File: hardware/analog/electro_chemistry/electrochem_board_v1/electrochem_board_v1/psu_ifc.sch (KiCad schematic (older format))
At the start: 1 part

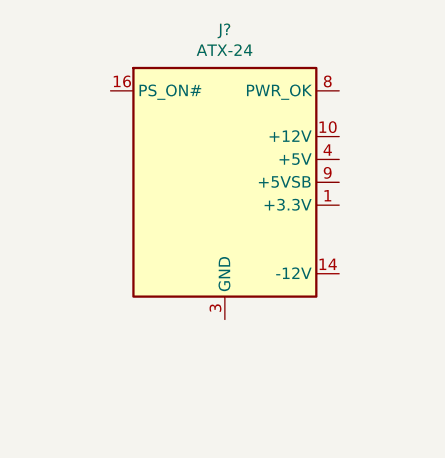
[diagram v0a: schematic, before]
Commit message: Electrochemistry board: preparing the layout
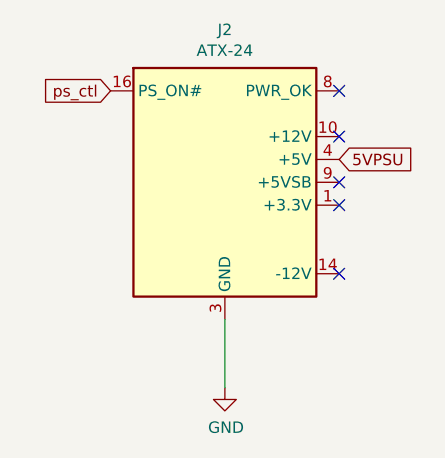
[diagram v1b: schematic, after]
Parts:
- J2: renamed from J?; footprint (none) -> Connector_Molex:Molex_Mini-Fit_Jr_5566-24A_2x12_P4.20mm_Vertical
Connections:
- net GND: now reaches J2.15 (GND), J2.17 (GND), J2.18 (GND), J2.19 (GND), J2.24 (GND), J2.3 (GND), J2.5 (GND), J2.7 (GND)
- net ps_ctl: now reaches J2.16 (PS_ON#)
- net 5VPSU: now reaches J2.21 (+5V), J2.22 (+5V), J2.23 (+5V), J2.4 (+5V), J2.6 (+5V)
- no-connect marks 0 -> 5
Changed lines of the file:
@@
 $EndDescr
 $Comp
-L Connector:ATX-24 J?
+L Connector:ATX-24 J2
 U 1 1 60970A62
 P 3900 3300
-F 0 "J?" H 3900 3967 50  0000 C CNN
+F 0 "J2" H 3900 3967 50  0000 C CNN
 F 1 "ATX-24" H 3900 3876 50  0000 C CNN
-F 2 "" H 3900 3200 50  0001 C CNN
+F 2 "Connector_Molex:Molex_Mini-Fit_Jr_5566-24A_2x12_P4.20mm_Vertical" H 3900 3200 50  0001 C CNN
 F 3 "https://www.intel.com/content/dam/www/public/us/en/documents/guides/power-supply-design-guide-june.pdf#page=33" H 6300 2750 50  0001 C CNN
 	1    3900 3300
 	1    0    0    -1
 $EndComp
+NoConn ~ 4400 3700
+NoConn ~ 4400 3100
+NoConn ~ 4400 3300
+NoConn ~ 4400 3400
+NoConn ~ 4400 2900
+Text GLabel 3400 2900 0    50   Input ~ 0
+ps_ctl
+Text GLabel 4400 3200 2    50   Input ~ 0
+5VPSU
+$Comp
+L power:GND #PWR03
+U 1 1 60A0377E
+P 3900 4200
+F 0 "#PWR03" H 3900 3950 50  0001 C CNN
+F 1 "GND" H 3905 4027 50  0000 C CNN
+F 2 "" H 3900 4200 50  0001 C CNN
+F 3 "" H 3900 4200 50  0001 C CNN
+	1    3900 4200
+	1    0    0    -1
+$EndComp
+Wire Wire Line
+	3900 3900 3900 4200
 $EndSCHEMATC

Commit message: elchem board STB improvement started
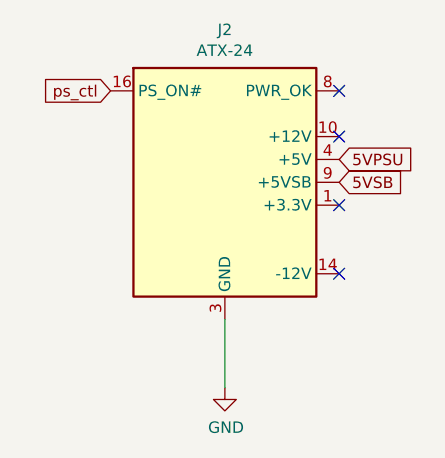
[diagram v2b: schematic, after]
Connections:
- net 5VSB: now reaches J2.9 (+5VSB)
- no-connect marks 5 -> 4
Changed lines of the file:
@@
 NoConn ~ 4400 3700
 NoConn ~ 4400 3100
-NoConn ~ 4400 3300
 NoConn ~ 4400 3400
 NoConn ~ 4400 2900
@@
 Wire Wire Line
 	3900 3900 3900 4200
+Text GLabel 4400 3300 2    50   Input ~ 0
+5VSB
 $EndSCHEMATC
